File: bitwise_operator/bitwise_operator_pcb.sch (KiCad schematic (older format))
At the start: 1 part, among them J1 Conn_01x03

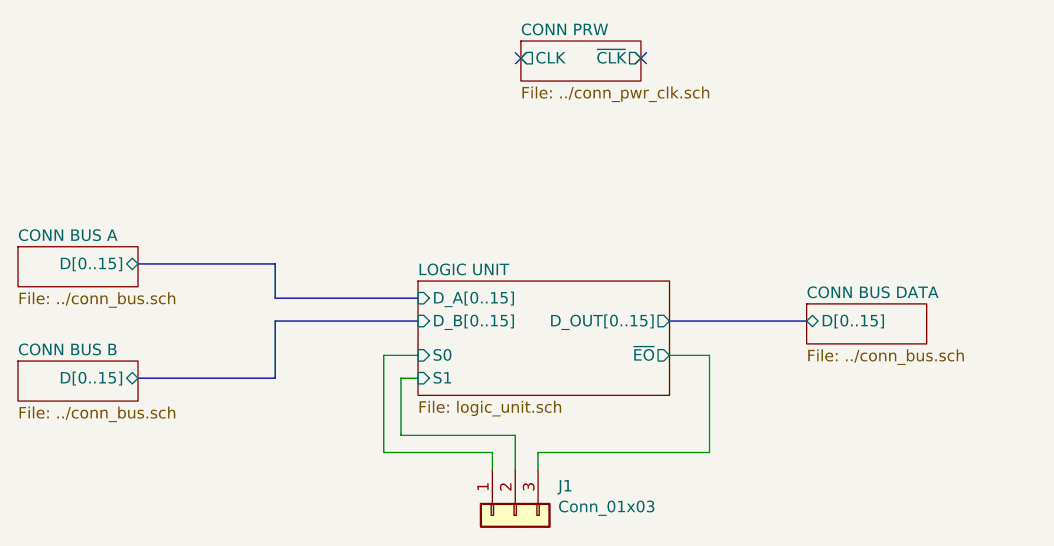
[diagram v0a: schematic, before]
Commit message: add bit operations
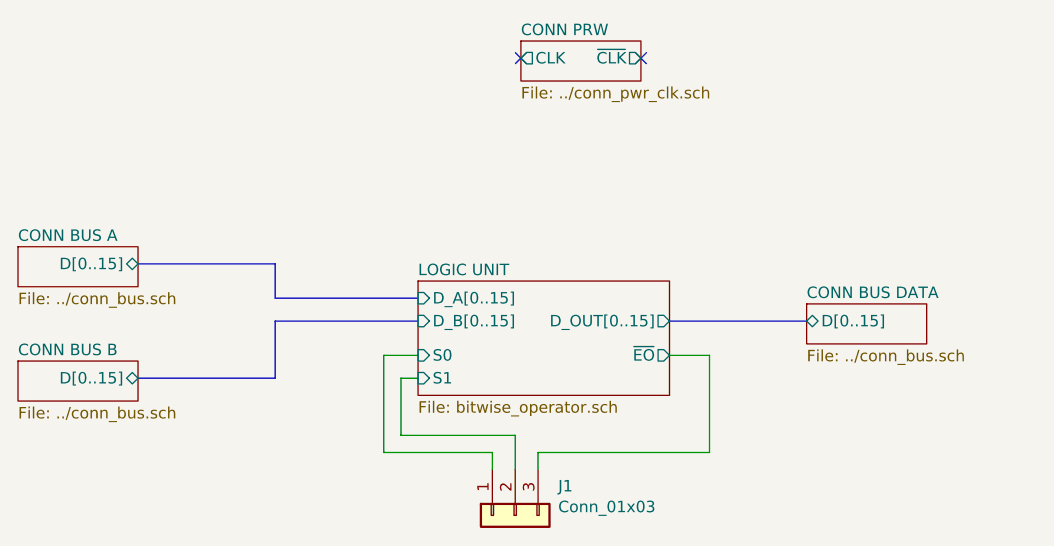
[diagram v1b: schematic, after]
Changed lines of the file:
@@
 EESchema Schematic File Version 4
+LIBS:bitwise_operator_pcb-cache
 EELAYER 30 0
 EELAYER END
@@
 U 5F0D7DA0
 F0 "LOGIC UNIT" 50
-F1 "logic_unit.sch" 50
+F1 "bitwise_operator.sch" 50
 F2 "D_A[0..15]" I L 4600 3000 50
 F3 "D_B[0..15]" I L 4600 3100 50

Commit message: memory programmer and cu
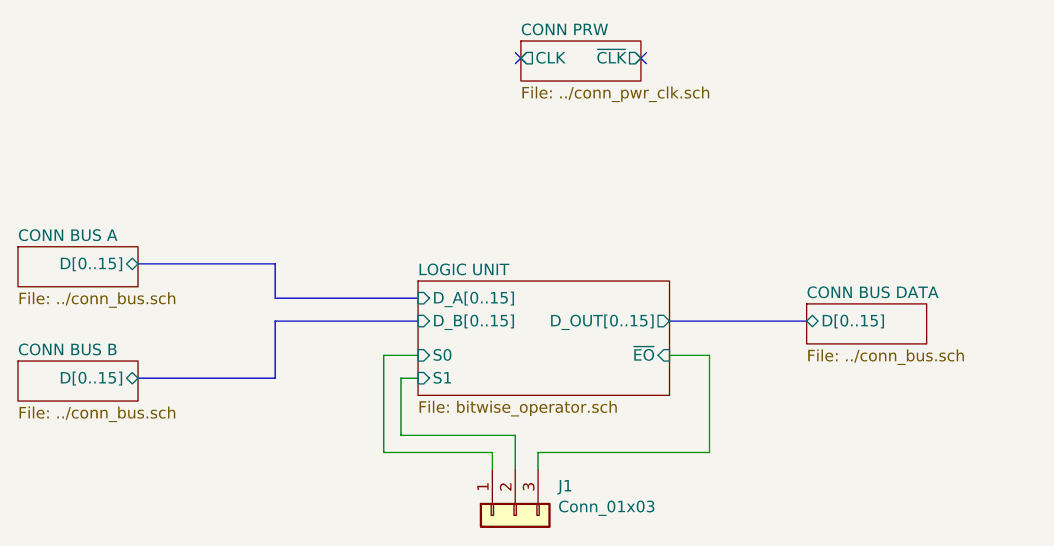
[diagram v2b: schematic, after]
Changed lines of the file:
@@
 F5 "S1" I L 4600 3350 50
 F6 "D_OUT[0..15]" O R 5700 3100 50
-F7 "~EO~" O R 5700 3250 50
+F7 "~EO~" I R 5700 3250 50
 $EndSheet
 $Sheet
